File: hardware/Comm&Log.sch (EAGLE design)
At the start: 25 parts, among them J1 DM3AT-SF-PEJM5, U1 S25FL116K0XMFI043, U2 CAT24M01

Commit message: Complete communication & logging board
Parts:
- removed J1: DM3AT-SF-PEJM5, dm3at-sf-pejm5:DM3AT-SF-PEJM5
- added C6: 0.1µF, rcl:C-EUC0603K
- added MICRO_SD: DM3AT-SF-PEJM5, dm3at-sf-pejm5:DM3AT-SF-PEJM5
- added R10, R11, R12, R9: 10k, resistor:R-US_R0603
- added R13, R14: 1k, resistor:R-US_R0603
- added R3: 10k, rcl:R-US_R0603
- added R4, R5, R6, R7, R8: 1k, rcl:R-US_R0603
- renumbered FC-1 to CRYSTAL, U$1 to ES920LR, U$3 to TWE-LITE, U1 to FLASH, U2 to EEPROM
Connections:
- removed net 920_USART_RX: ES920LR.PTA2/TX, STM32F001.PA10/USART1_RX/TIM1_CH3
- removed net 920_USART_TX: ES920LR.PTA1/RX, STM32F001.PA9/USART1_TX/TIM1_CH2
- removed net I2C1_SCL: EEPROM.SCL, STM32F001.PB6USART1_TX/I2C1_SCL
- removed net I2C1_SDA: EEPROM.SDA, STM32F001.PB7/USART1_RX/I2C1_SDA
- removed net N$33: U$2.P14
- removed net N$34: U$2.P13
- removed net N$35: U$2.P12
- removed net N$36: U$2.P11
- removed net N$43: U$2.P10
- removed net N$44: U$2.P9
- removed net N$45: U$2.P8
- removed net N$46: U$2.P7
- removed net N$47: U$2.P6
- removed net N$48: U$2.P5
- removed net N$49: U$2.P4
- removed net N$50: U$2.P3
- removed net N$56: STM32F001.PA5/ADC_IN5/DAC_OUT2/SPI1_SCK
- removed net N$57: STM32F001.PA6/ADC_IN6/SPI1_MISO/TIM3_CH1
- removed net N$58: STM32F001.PA7/ADC_IN7/SPI1_MOSI/TIM3_CH2
- removed net N$61: STM32F001.PA12/USB_DP/CAN_TX
- removed net N$65: STM32F001.PB10/I2C2_SCL/TIM2_CH3/USART3_TX
- removed net N$66: J1.A, STM32F001.PB11/I2C2_SDA/TIM2_C4/USART3_RX
- removed net SPI1_MISO: J1.DAT0, STM32F001.PB4/SPI1_MISO/TIM3_CH1
- removed net SPI1_MOSI: J1.CMD, STM32F001.PB5/WKUP6/SPI1_MOSI/TIM3_CH2
- removed net SPI1_NSS: J1.CD/DAT3, STM32F001.PA15/USART2_RX
- removed net SPI1_SCK: J1.CLK, STM32F001.PB3/SPI1_SCK/TIM2_CH2
- removed net SPI2_MISO: FLASH.SO(IO1), STM32F001.PB14/SPI2_MISO/I2C2_SDA
- removed net SPI2_MOSI: FLASH.SI(IO0), STM32F001.PB15/WKUP7/RTC_REFIN/SPI2_MOSI
- removed net SPI2_NSS: FLASH.CS#, STM32F001.PB12
- removed net SPI2_SCK: FLASH.SCK, STM32F001.PB13/SPI2_SCK/I2C2_SCL
- removed net TWE_USART_RX: STM32F001.PA3/ADC_IN3/COMP2_INP/USART2_RX, TWE-LITE.DIO6
- removed net TWE_USART_TX: STM32F001.PA2/ADC_IN2/WKUP4USART2_TX, TWE-LITE.DIO7
- new net 920_!SLEEP!': R14.1, STM32F001.PA8/TIM1_CH1
- new net 920_RTX: ES920LR.PTA2/TX, R7.1, STM32F001.PA10/USART1_RX/TIM1_CH3
- new net 920_TRX: ES920LR.PTA1/RX, R8.1, STM32F001.PA9/USART1_TX/TIM1_CH2
- new net EEPROM_SCL: EEPROM.SCL, R9.1, STM32F001.PB10/I2C2_SCL/TIM2_CH3/USART3_TX, U$2.P9
- new net EEPROM_SDA: EEPROM.SDA, R10.1, STM32F001.PB11/I2C2_SDA/TIM2_C4/USART3_RX, U$2.P10
- new net FLASH_MISO: FLASH.SO(IO1), STM32F001.PA6/ADC_IN6/SPI1_MISO/TIM3_CH1, U$2.P13
- new net FLASH_MOSI: FLASH.SI(IO0), STM32F001.PA7/ADC_IN7/SPI1_MOSI/TIM3_CH2, U$2.P11
- new net FLASH_SCK: FLASH.SCK, STM32F001.PA5/ADC_IN5/DAC_OUT2/SPI1_SCK, U$2.P12
- new net N$1: ES920LR.RESETB
- new net N$3: R4.1, STM32F001.PA11/USB_DM/CAN_RX
- new net N$4: R6.2, U$2.P2
- new net N$5: R7.2, U$2.P5
- new net N$6: R13.1, STM32F001.PB3/SPI1_SCK/TIM2_CH2
- new net SD_!SS!: MICRO_SD.CD/DAT3
- new net SD_!SW!: MICRO_SD.A, R3.2, STM32F001.PA2/ADC_IN2/WKUP4USART2_TX
- new net SD_MISO: MICRO_SD.DAT0, STM32F001.PB14/SPI2_MISO/I2C2_SDA
- new net SD_MOSI: MICRO_SD.CMD, STM32F001.PB15/WKUP7/RTC_REFIN/SPI2_MOSI
- new net SD_SCK: MICRO_SD.CLK, STM32F001.PB13/SPI2_SCK/I2C2_SCL
- new net TWE_BPS: STM32F001.PA12/USB_DP/CAN_TX, TWE-LITE.DIO17
- new net TWE_RTX: R5.1, STM32F001.PB7/USART1_RX/I2C1_SDA, TWE-LITE.DIO6
- new net TWE_TRX: R6.1, STM32F001.PB6USART1_TX/I2C1_SCL, TWE-LITE.DIO7
- net 920_!SLEEP!: now also R11.1, R14.2, U$2.P8
- net GND: now also C6.2, FLASH.CS#, MICRO_SD.B, MICRO_SD.SHIELD, MICRO_SD.VSS, R1.1; no longer J1.B, J1.SHIELD, J1.VSS
- net N$2: now also R8.2, U$2.P7; no longer EEPROM.A0
- net N$73: now also STM32F001.PA1/ADC_IN1/COMP1_INP/USART4_RX
- net N$74: now also R5.2
- net TWE_!PGM!: now also STM32F001.PB4/SPI1_MISO/TIM3_CH1; no longer STM32F001.PA0/USART4_TX/WKUP1/ADC_IN0
- net TWE_!RESET!: now also R1.2, R4.2, U$2.P6; no longer R1.1, STM32F001.PA4/ADC_IN4/DAC_OUT1
- net TWE_!RTS!: now also STM32F001.PB5/WKUP6/SPI1_MOSI/TIM3_CH2; no longer STM32F001.PA1/ADC_IN1/COMP1_INP/USART4_RX
- net TWE_SLEEP: now also R12.1, R13.2, U$2.P4; no longer U$2.P2
- net VDD: now also C6.1, MICRO_SD.VDD, R10.2, R11.2, R12.2, R3.1, R9.2; no longer J1.VDD, R1.2
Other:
- moved on the sheet: C1, C4, R1

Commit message: Some fixes
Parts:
- C12: value (none) -> 0.1µF
- R2: value (none) -> 470
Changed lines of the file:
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@@
 <?xml version="1.0" encoding="utf-8"?>
 <!DOCTYPE eagle SYSTEM "eagle.dtd">
-<eagle version="9.5.1">
+<eagle version="9.5.2">
 <drawing>
 <settings>
@@
 <part name="VDD11" library="supply1" library_urn="urn:adsk.eagle:library:371" deviceset="VDD" device=""/>
 <part name="VDD12" library="supply1" library_urn="urn:adsk.eagle:library:371" deviceset="VDD" device=""/>
-<part name="C12" library="rcl" library_urn="urn:adsk.eagle:library:334" deviceset="C-EU" device="C0603K" package3d_urn="urn:adsk.eagle:package:23680/2"/>
+<part name="C12" library="rcl" library_urn="urn:adsk.eagle:library:334" deviceset="C-EU" device="C0603K" package3d_urn="urn:adsk.eagle:package:23680/2" value="0.1µF"/>
 <part name="VDD13" library="supply1" library_urn="urn:adsk.eagle:library:371" deviceset="VDD" device=""/>
 <part name="LED1" library="led" library_urn="urn:adsk.eagle:library:259" deviceset="LED" device="CHIP-LED0603" package3d_urn="urn:adsk.eagle:package:15819/3"/>
@@
 <part name="CL4" library="rcl" library_urn="urn:adsk.eagle:library:334" deviceset="C-EU" device="C0603K" package3d_urn="urn:adsk.eagle:package:23680/2" value="15pF"/>
 <part name="GND9" library="supply1" library_urn="urn:adsk.eagle:library:371" deviceset="GND" device=""/>
-<part name="R2" library="rcl" library_urn="urn:adsk.eagle:library:334" deviceset="R-US_" device="R0603" package3d_urn="urn:adsk.eagle:package:23555/3"/>
+<part name="R2" library="rcl" library_urn="urn:adsk.eagle:library:334" deviceset="R-US_" device="R0603" package3d_urn="urn:adsk.eagle:package:23555/3" value="470"/>
 <part name="VDD14" library="supply1" library_urn="urn:adsk.eagle:library:371" deviceset="VDD" device=""/>
 <part name="GND10" library="supply1" library_urn="urn:adsk.eagle:library:371" deviceset="GND" device=""/>

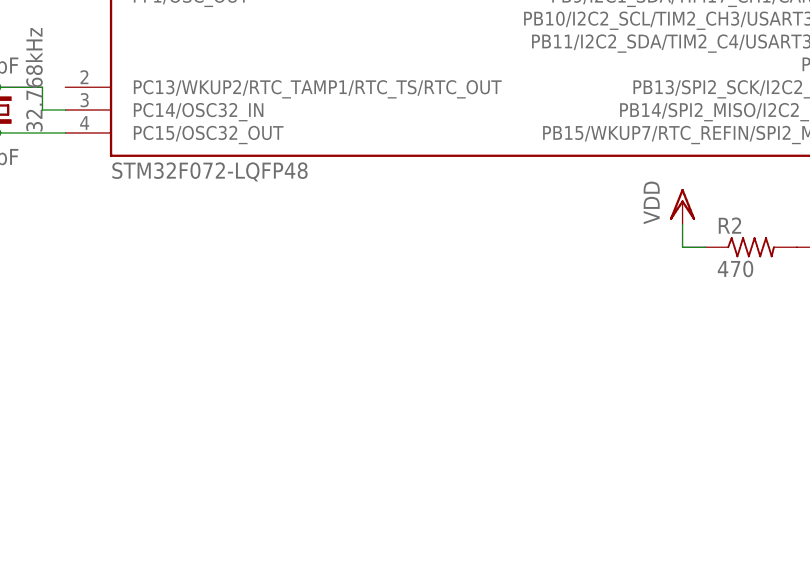
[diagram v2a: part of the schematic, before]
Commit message: Update CAN command channel
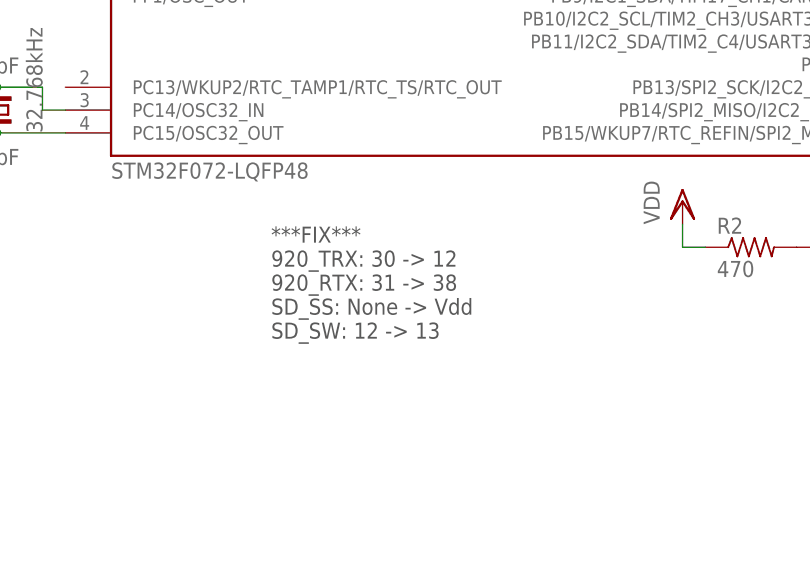
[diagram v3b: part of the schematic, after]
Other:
- note added: "***FIX*** 920_TRX: 30 -> 12 920_RTX: 31 -> 38 SD_SS: None -> Vdd SD_SW: 12 -> 13"
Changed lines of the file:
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@@
 <?xml version="1.0" encoding="utf-8"?>
 <!DOCTYPE eagle SYSTEM "eagle.dtd">
-<eagle version="9.5.2">
+<eagle version="9.6.2">
 <drawing>
 <settings>
@@
 <sheet>
 <plain>
+<text x="50.8" y="-7.62" size="1.778" layer="97">***FIX***
+920_TRX: 30 -&gt; 12
+920_RTX: 31 -&gt; 38
+SD_SS: None -&gt; Vdd
+SD_SW: 12 -&gt; 13</text>
 </plain>
 <instances>
@@
 </drawing>
 <compatibility>
+<note version="6.3" minversion="6.2.2" severity="warning">
+Since Version 6.2.2 text objects can contain more than one line,
+which will not be processed correctly with this version.
+</note>
 <note version="8.2" severity="warning">
 Since Version 8.2, EAGLE supports online libraries. The ids

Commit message: WIP
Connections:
- net N$1 renamed 920_!RESET!
- net N$2 renamed 920_TRX_
- net N$5 renamed 920_RTX_
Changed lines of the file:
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@@
 <attribute name="VALUE" x="193.04" y="66.04" size="1.778" layer="96"/>
 </instance>
-<instance part="GND3" gate="1" x="266.7" y="68.58" smashed="yes">
-<attribute name="VALUE" x="264.16" y="66.04" size="1.778" layer="96"/>
+<instance part="GND3" gate="1" x="274.32" y="68.58" smashed="yes">
+<attribute name="VALUE" x="271.78" y="66.04" size="1.778" layer="96"/>
 </instance>
 <instance part="GND4" gate="1" x="238.76" y="-40.64" smashed="yes">
@@
 <segment>
 <pinref part="ES920LR" gate="G$1" pin="GND@26"/>
-<wire x1="251.46" y1="73.66" x2="266.7" y2="73.66" width="0.1524" layer="91"/>
-<wire x1="266.7" y1="73.66" x2="266.7" y2="71.12" width="0.1524" layer="91"/>
+<wire x1="251.46" y1="73.66" x2="274.32" y2="73.66" width="0.1524" layer="91"/>
+<wire x1="274.32" y1="73.66" x2="274.32" y2="71.12" width="0.1524" layer="91"/>
 <pinref part="GND3" gate="1" pin="GND"/>
 </segment>
@@
 </segment>
 </net>
-<net name="N$1" class="0">
+<net name="920_!RESET!" class="0">
 <segment>
 <pinref part="ES920LR" gate="G$1" pin="RESETB"/>
 <wire x1="251.46" y1="68.58" x2="254" y2="68.58" width="0.1524" layer="91"/>
-</segment>
-</net>
-<net name="N$2" class="0">
+<label x="254" y="68.58" size="1.778" layer="95" xref="yes"/>
+</segment>
+</net>
+<net name="920_TRX_" class="0">
 <segment>
 <pinref part="R8" gate="G$1" pin="2"/>
@@
 </segment>
 </net>
-<net name="N$5" class="0">
+<net name="920_RTX_" class="0">
 <segment>
 <pinref part="R7" gate="G$1" pin="2"/>
